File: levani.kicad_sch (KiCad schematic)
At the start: 10 parts, among them M1 Motor_DC, Q1 NPN, SW1 SW_Push

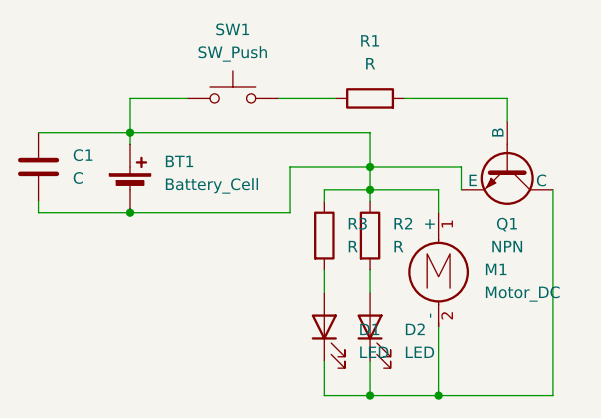
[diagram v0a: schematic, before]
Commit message: fix schematic and add more silkscreened text
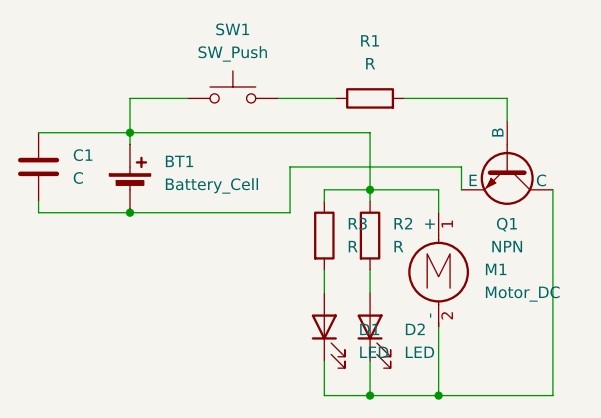
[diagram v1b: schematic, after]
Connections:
- net at BT1.1 (+), C1.1, M1.1 (+)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: no longer BT1.2 (-), C1.2, Q1.3 (E)
- new net: BT1.2 (-), C1.2, Q1.3 (E)
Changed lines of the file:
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@@
-	)
-	(junction
-		(at 59.69 63.5)
-		(diameter 0)
-		(color 0 0 0 0)
 	)
 	(junction
@@
 	(wire
 		(pts
-			(xy 50.8 63.5) (xy 59.69 63.5)
+			(xy 50.8 63.5) (xy 69.85 63.5)
 		)
 		(stroke
@@
 	(wire
 		(pts
-			(xy 59.69 66.04) (xy 59.69 63.5)
+			(xy 59.69 59.69) (xy 59.69 66.04)
 		)
 		(stroke
@@
 	(wire
 		(pts
-			(xy 59.69 63.5) (xy 59.69 59.69)
-		)
-		(stroke
-			(width 0)
-			(type default)
-		)
-	)
-	(wire
-		(pts
 			(xy 59.69 74.93) (xy 59.69 77.47)
 		)
@@
 		)
 		(stroke
-			(width 0)
-			(type default)
-		)
-	)
-	(wire
-		(pts
-			(xy 69.85 63.5) (xy 59.69 63.5)
-		)
-		(stroke
